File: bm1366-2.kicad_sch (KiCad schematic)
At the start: 88 parts, among them U1 25MHz, U13 ADP171AUJ-R7, U18 TLV3544, U19 BM1366_mode0, U22 BM1366_mode0, U23 ADP171AUJ-R7

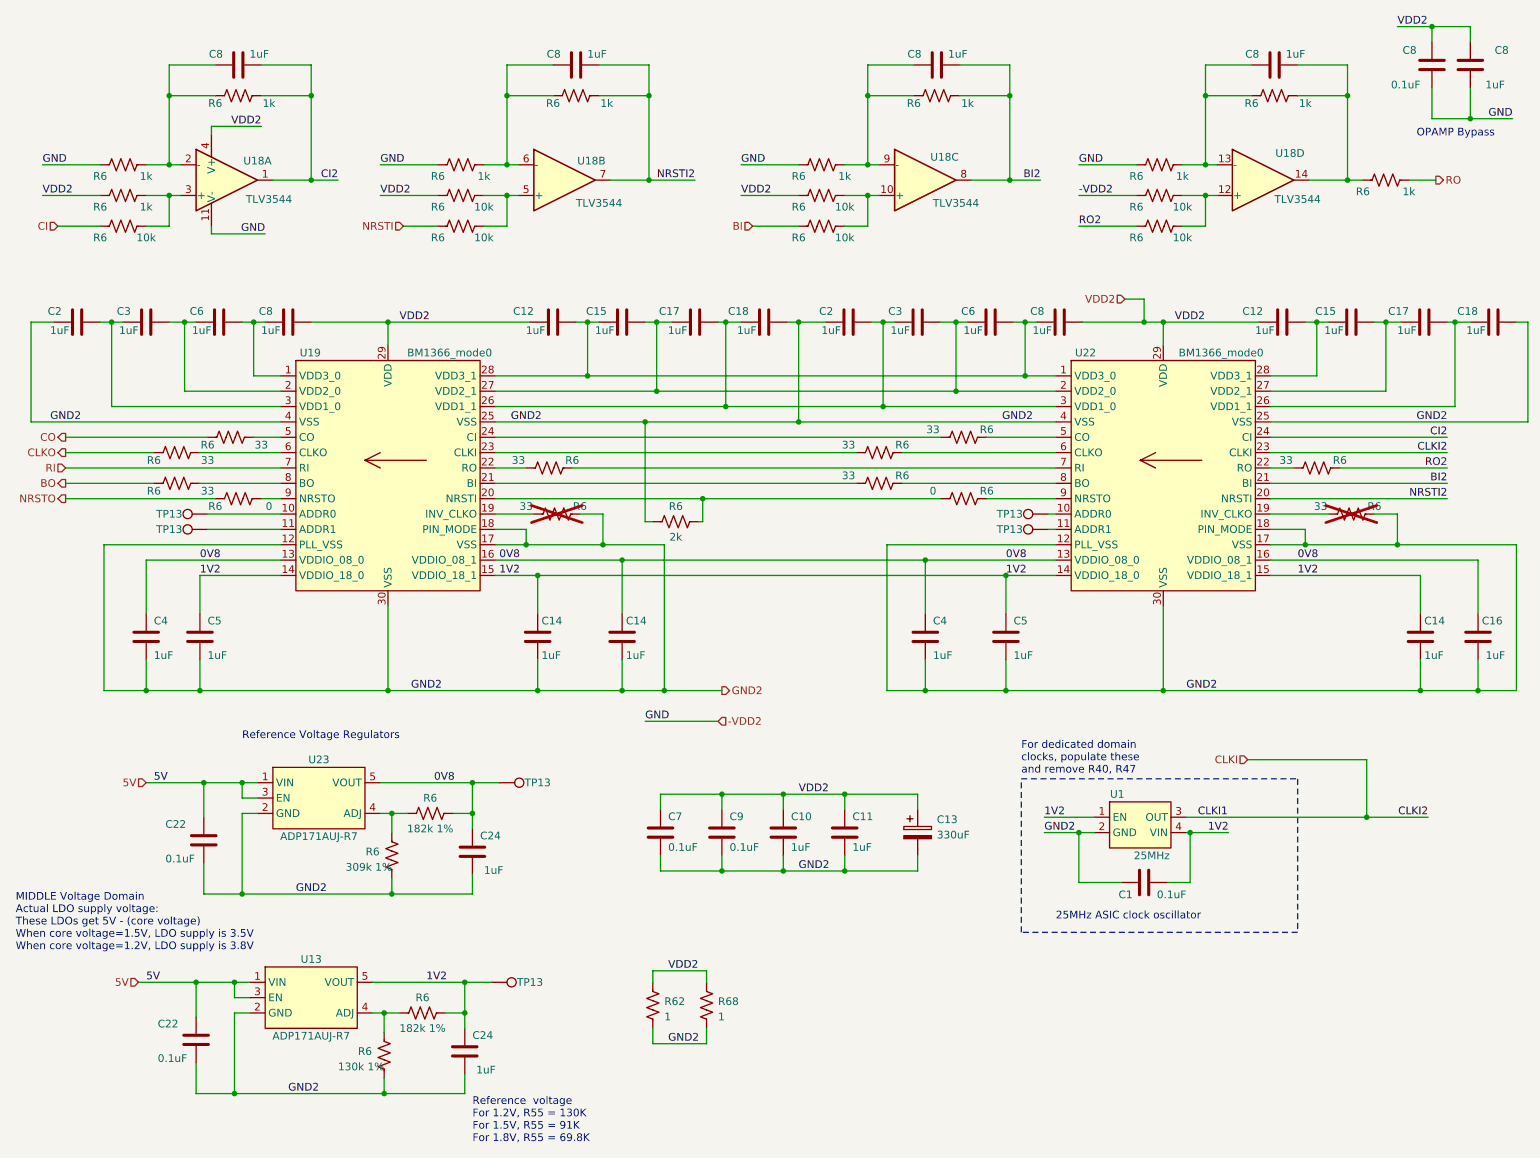
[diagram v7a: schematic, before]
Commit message: updated 1V2 to 1V8 and updated the BOM
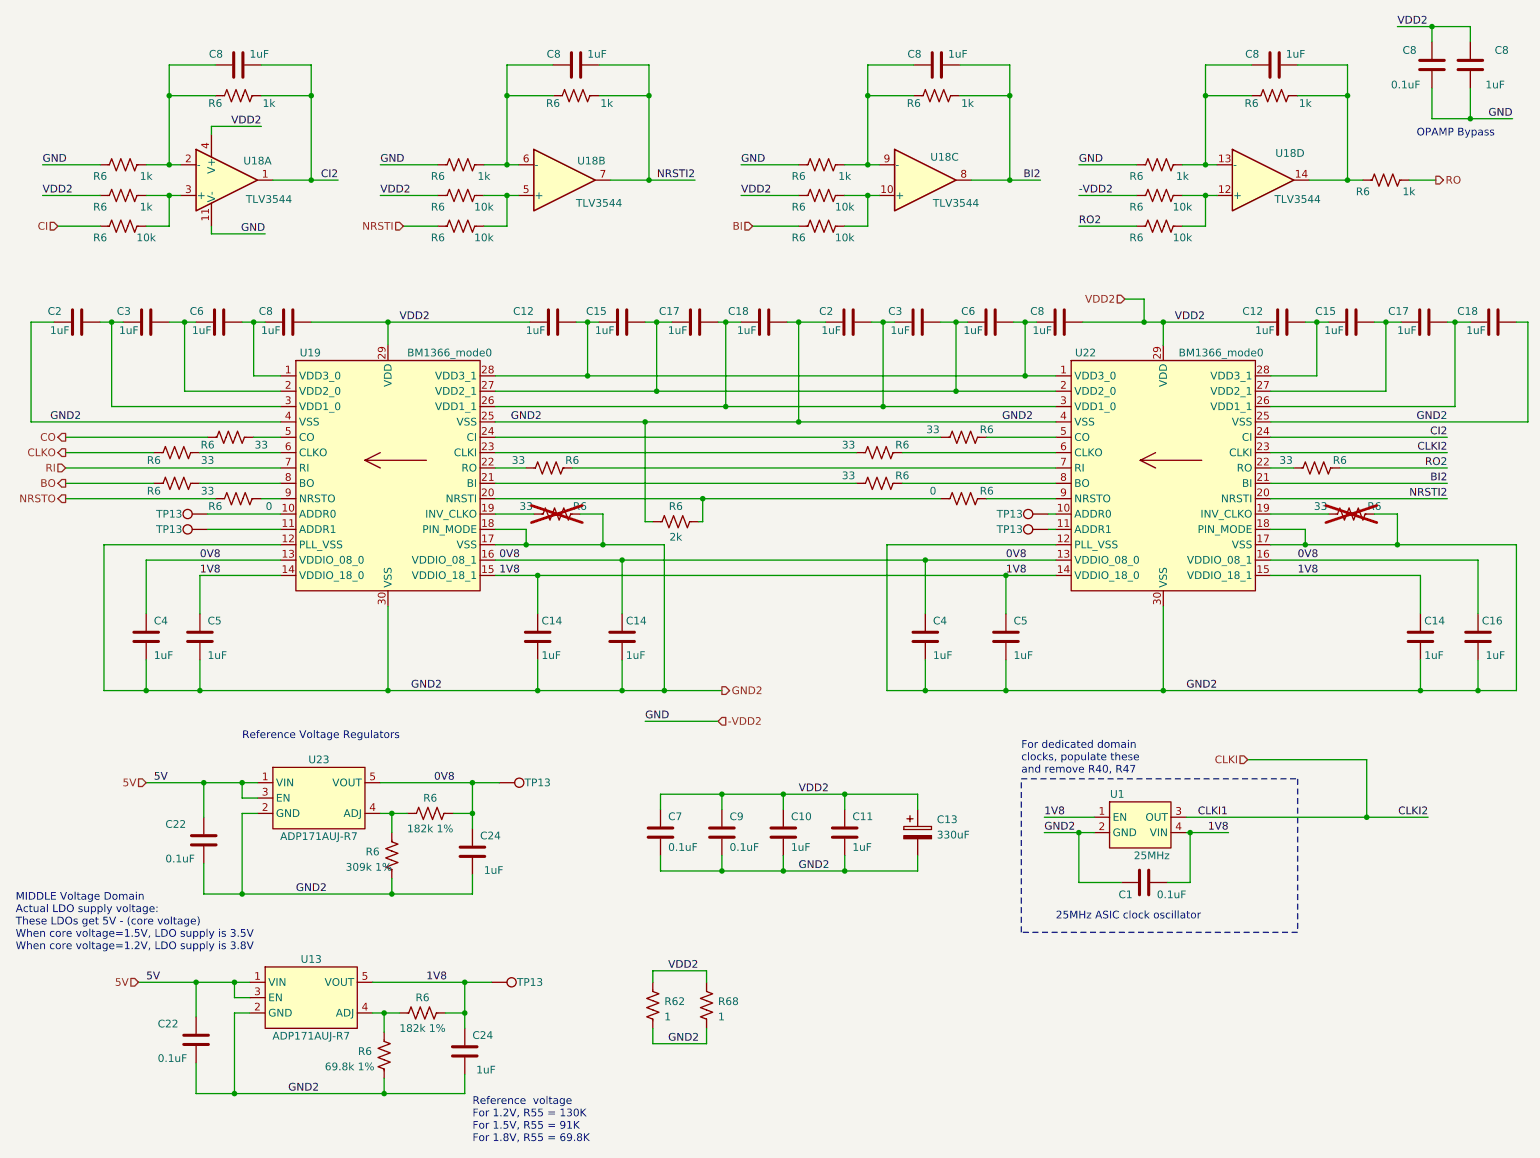
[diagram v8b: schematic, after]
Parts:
- R6: value 130k 1% -> 69.8k 1%; DK YAG2969CT-ND -> YAG3216CT-ND; PARTNO RC0402FR-07130KL -> RC0402FR-0769K8L
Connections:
- net 1V2 renamed 1V8
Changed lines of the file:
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@@
     (effects (font (size 1.27 1.27)) (justify left bottom))
   )
-  (label "1V2" (at 95.885 108.585 0) (fields_autoplaced)
+  (label "1V8" (at 95.885 108.585 0) (fields_autoplaced)
     (effects (font (size 1.27 1.27)) (justify left bottom))
   )
@@
     (effects (font (size 1.27 1.27)) (justify right bottom))
   )
-  (label "1V2" (at 83.82 175.895 0) (fields_autoplaced)
+  (label "1V8" (at 83.82 175.895 0) (fields_autoplaced)
     (effects (font (size 1.27 1.27)) (justify left bottom))
   )
@@
     (effects (font (size 1.27 1.27)) (justify left bottom))
   )
-  (label "1V2" (at 216.535 151.13 180) (fields_autoplaced)
+  (label "1V8" (at 216.535 151.13 180) (fields_autoplaced)
     (effects (font (size 1.27 1.27)) (justify right bottom))
   )
@@
     (effects (font (size 1.27 1.27)) (justify left bottom))
   )
-  (label "1V2" (at 186.055 148.59 0) (fields_autoplaced)
+  (label "1V8" (at 186.055 148.59 0) (fields_autoplaced)
     (effects (font (size 1.27 1.27)) (justify left bottom))
   )
@@
     (effects (font (size 1.27 1.27)) (justify left bottom))
   )
-  (label "1V2" (at 227.965 108.585 0) (fields_autoplaced)
+  (label "1V8" (at 227.965 108.585 0) (fields_autoplaced)
     (effects (font (size 1.27 1.27)) (justify left bottom))
   )
@@
     (effects (font (size 1.27 1.27)) (justify left bottom))
   )
-  (label "1V2" (at 46.355 108.585 0) (fields_autoplaced)
+  (label "1V8" (at 46.355 108.585 0) (fields_autoplaced)
     (effects (font (size 1.27 1.27)) (justify left bottom))
   )
@@
     (effects (font (size 1.27 1.27)) (justify left bottom))
   )
-  (label "1V2" (at 179.705 108.585 0) (fields_autoplaced)
+  (label "1V8" (at 179.705 108.585 0) (fields_autoplaced)
     (effects (font (size 1.27 1.27)) (justify left bottom))
   )
@@
       (effects (font (size 1.27 1.27)))
     )
-    (property "Value" "130k 1%" (at 73.025 189.865 0)
+    (property "Value" "69.8k 1%" (at 71.12 189.865 0)
       (effects (font (size 1.27 1.27)))
     )
@@
       (effects (font (size 1.27 1.27)) hide)
     )
-    (property "DK" "YAG2969CT-ND" (at 76.835 187.96 0)
-      (effects (font (size 1.27 1.27)) hide)
-    )
-    (property "PARTNO" "RC0402FR-07130KL" (at 76.835 187.96 0)
-      (effects (font (size 1.27 1.27)) hide)
-    )
+    (property "DK" "YAG3216CT-ND" (at 76.835 187.96 0)
+      (effects (font (size 1.27 1.27)) hide)
+    )
+    (property "PARTNO" "RC0402FR-0769K8L" (at 76.835 187.96 0)
+      (effects (font (size 1.27 1.27)) hide)
+    )
